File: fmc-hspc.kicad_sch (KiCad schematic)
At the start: 60 parts, among them J18 ASP-184329-01_mounting_holes_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

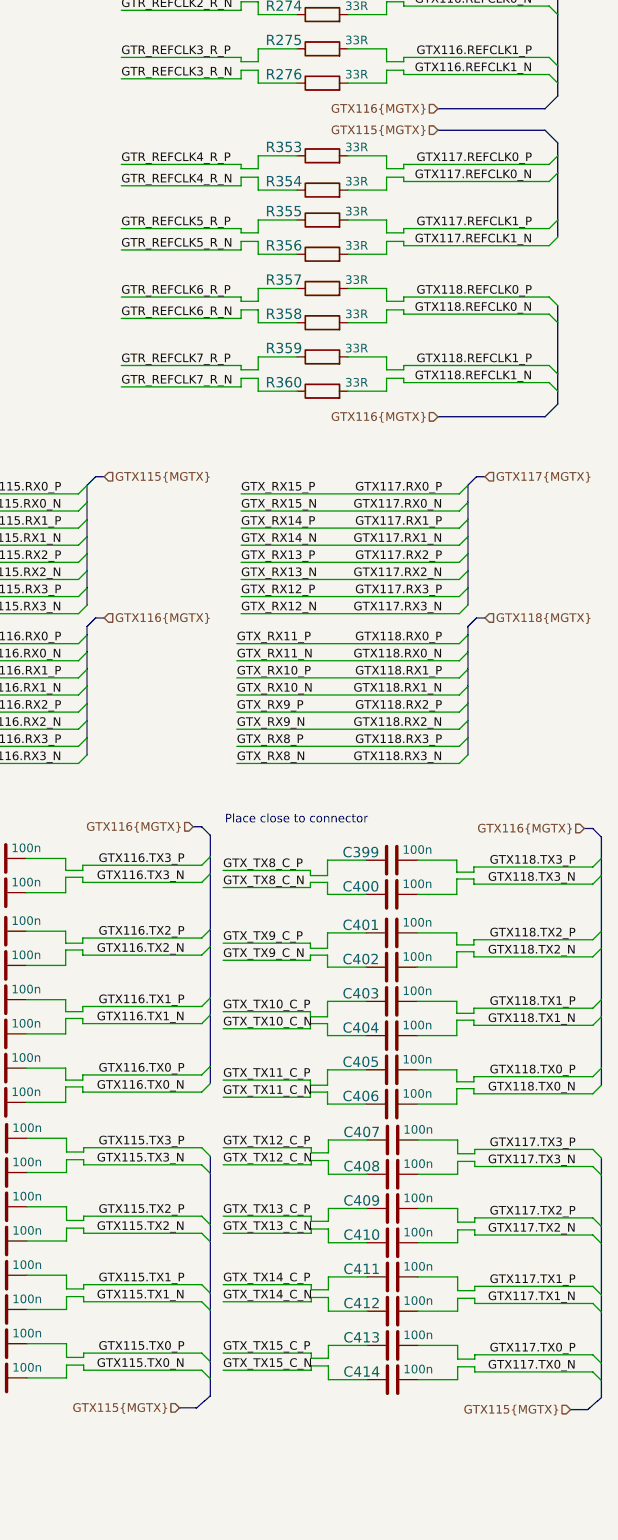
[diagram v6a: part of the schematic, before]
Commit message: Working on final fixes on PCIe interface signals
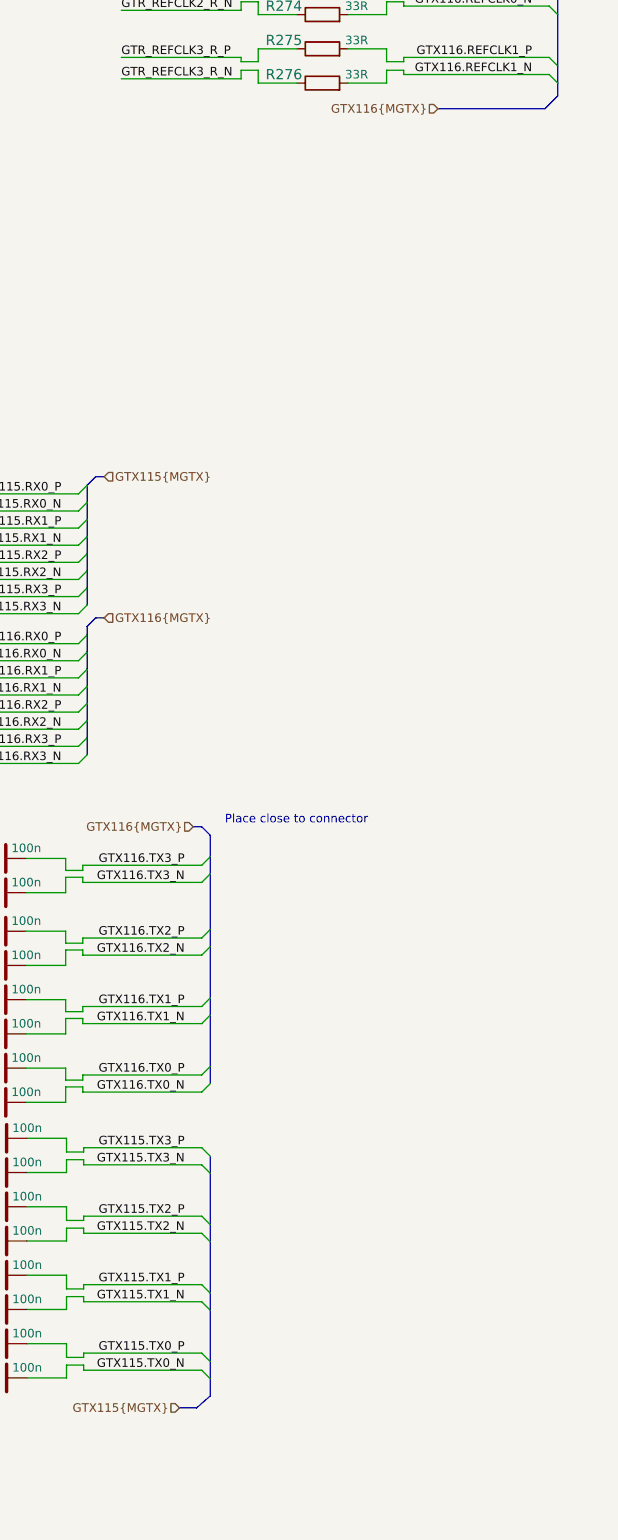
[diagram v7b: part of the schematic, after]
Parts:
- removed C399, C400, C401, C402, C403, C404, C405, C406, C407, C408, C409, C410, C411, C412, C413, C414: C_100n_0402, antmicro-footprints:0402-cap, symbol antmicroCapacitors0402:C_100n_0402
- removed R353, R354, R355, R356, R357, R358, R359, R360: R_33R_0402, antmicro-footprints:0402-res, symbol antmicroResistors0402:R_33R_0402
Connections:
- net GTX117.RX0_N renamed GTX_RX15_N
- net GTX117.RX0_P renamed GTX_RX15_P
- net GTX117.RX1_N renamed GTX_RX14_N
- net GTX117.RX1_P renamed GTX_RX14_P
- net GTX117.RX2_N renamed GTX_RX13_N
- net GTX117.RX2_P renamed GTX_RX13_P
- net GTX117.RX3_N renamed GTX_RX12_N
- net GTX117.RX3_P renamed GTX_RX12_P
- net GTX118.RX0_N renamed GTX_RX11_N
- net GTX118.RX0_P renamed GTX_RX11_P
- net GTX118.RX1_N renamed GTX_RX10_N
- net GTX118.RX1_P renamed GTX_RX10_P
- net GTX118.RX2_N renamed GTX_RX9_N
- net GTX118.RX2_P renamed GTX_RX9_P
- net GTX118.RX3_N renamed GTX_RX8_N
- net GTX118.RX3_P renamed GTX_RX8_P

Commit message: Update signage
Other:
- moved on the sheet: C296, C297, C298, C299, C300, C301, C302, C303, C304, C305, C306, C307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
